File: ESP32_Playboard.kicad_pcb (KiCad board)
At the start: 4 copper layers, 50.3 x 50.8 mm, 42 parts, among them J1 USB_B_Micro, J2 TF_PUSH, Q1 Q_NPN_BEC, Q2 Q_NPN_BEC, Q3 Q_NPN_BEC, SW1 SW_SPST, SW2 SW_SPST, U1 AMS1117-3.3, U2 USBLC6-2SC6, U3 CH340G, U4 MPU-6050, U5 ESP32-WROVER-I, U6 SHT30-DIS, Y1 12MHz

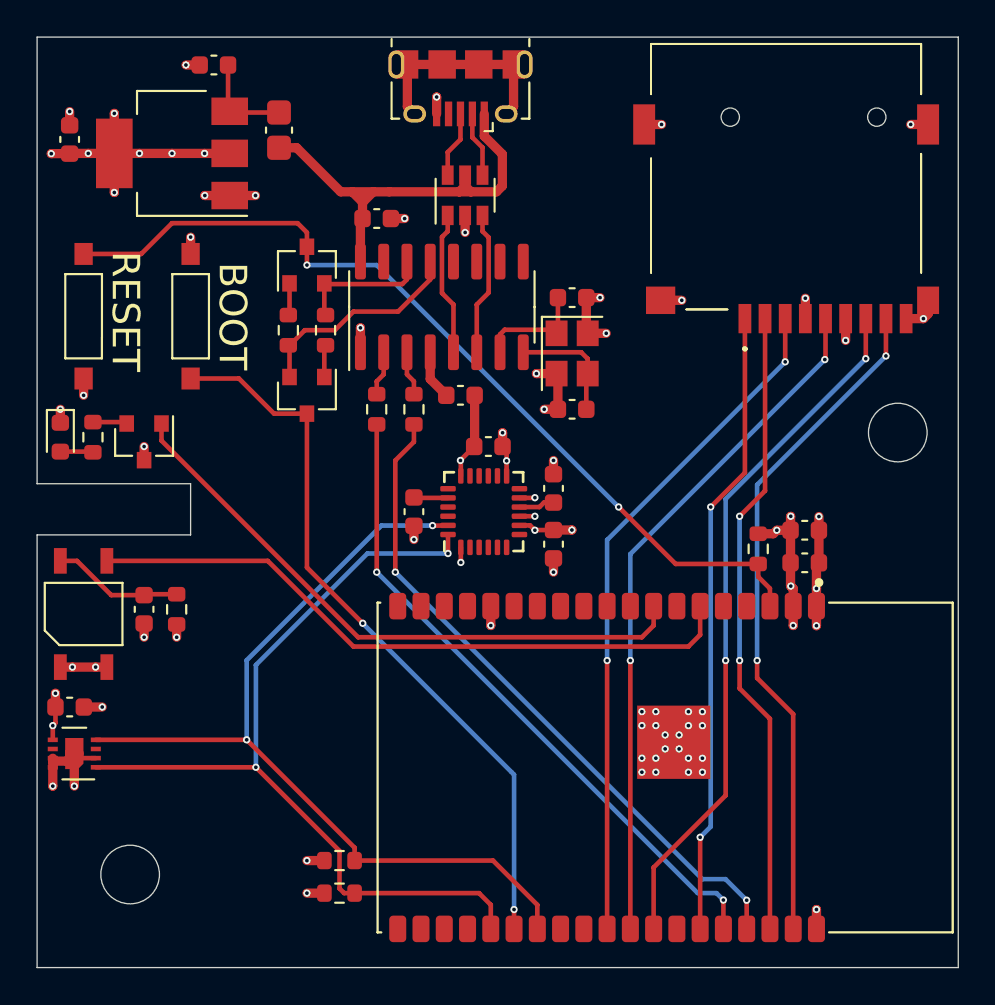
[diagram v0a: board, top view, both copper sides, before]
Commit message: Added magnetometer, attached interrupts, added silkscreen orientation
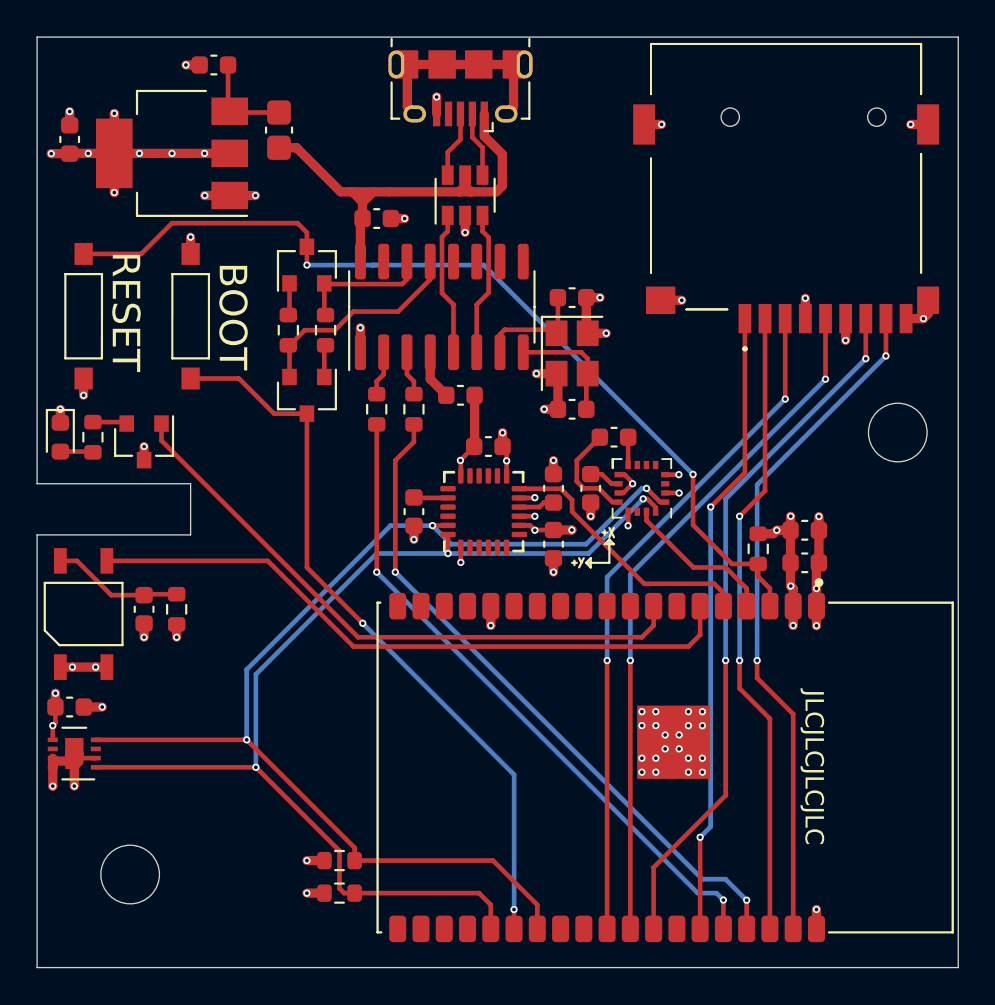
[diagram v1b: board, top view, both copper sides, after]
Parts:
- added C10: 4.7uF, Capacitor_SMD:C_0603_1608Metric, F.Cu at (120.7, 84.8)
- added C11: 220pF, Capacitor_SMD:C_0603_1608Metric, F.Cu at (121.9, 82.0)
- added U4: QMC5883L, Package_LGA:LGA-16_3x3mm_P0.5mm, F.Cu at (123.4, 84.8)
- D2: value IR LED -> IR_LED
- renumbered C14 to C12, C12 to C13, C13 to C14, C10 to C15, C11 to C16, C8 to C7, C9 to C8, C7 to C9, H3 to H1, R9 to R8, R8 to R9, U4 to U5, U5 to U7
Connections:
- U7 pad 4: Net-(U5-Pad4) -> /QMC_INT
- U7 pad 5: Net-(U5-Pad5) -> /MPU_INT
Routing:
- net /MPU_INT: track 0.00 -> 14.6 mm
- net /I2C0_SCL: track 47.9 -> 62.3 mm, vias 2 -> 3
- net /I2C0_SDA: track 46.8 -> 59.5 mm, vias 2 -> 3
- net /QMC_INT: track 0.00 -> 8.45 mm
- net Net-(C11-Pad2): track 0.00 -> 5.68 mm
- net GND: track 52.5 -> 55.2 mm, vias 58 -> 60
- net /REG_3V3: track 34.4 -> 36.7 mm, vias 22 -> 25
- net /RESET: track 48.8 -> 50.7 mm
- net Net-(C10-Pad1): track 0.00 -> 1.74 mm
- net Net-(C11-Pad1): track 0.00 -> 1.52 mm
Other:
- board text added: "JLCJLCJLCJLC"
